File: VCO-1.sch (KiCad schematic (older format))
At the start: 72 parts

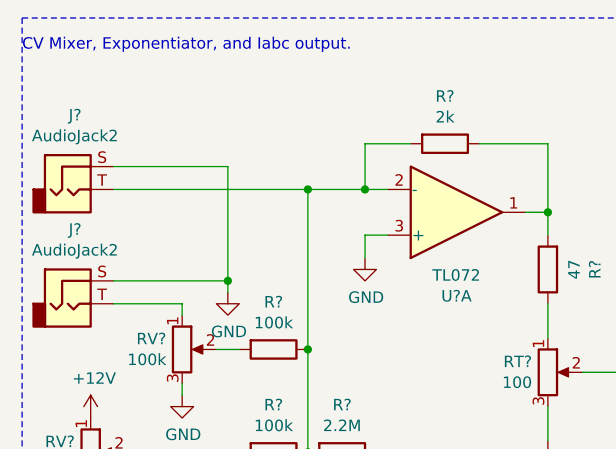
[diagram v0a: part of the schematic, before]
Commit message: Fixed missing input resistor for V/oct
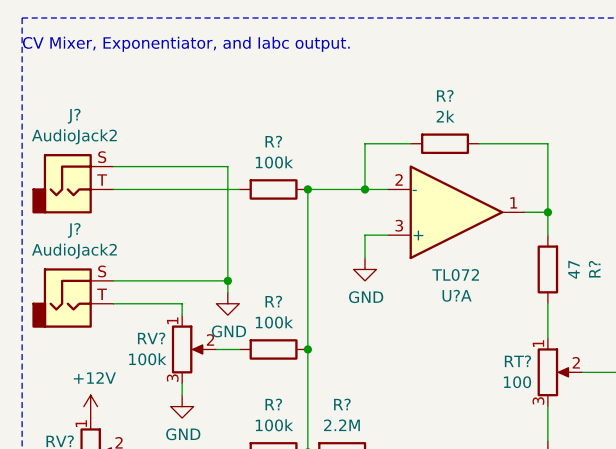
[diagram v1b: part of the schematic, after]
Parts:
- added R?: 100k, symbol Device:R
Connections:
- net at R?.1, R?.1, R?.1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: now also R?.1; no longer J?.T
- new net: J?.T, R?.2
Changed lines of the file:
@@
 	1    0    0    -1
 $EndComp
-Wire Wire Line
-	950  1550 1800 1550
 Connection ~ 1800 1550
 $Comp
@@
 Wire Wire Line
 	1450 1950 1450 2000
-Wire Wire Line
-	950  1450 1450 1450
-Wire Wire Line
-	1450 1450 1450 1950
-Connection ~ 1450 1950
 $Comp
 L power:GND #PWR?
@@
 Text Notes 10350 5450 0    50   ~ 0
 SAW OUT
+$Comp
+L Device:R R?
+U 1 1 604EF043
+P 1650 1550
+F 0 "R?" V 1443 1550 50  0000 C CNN
+F 1 "100k" V 1534 1550 50  0000 C CNN
+F 2 "" V 1580 1550 50  0001 C CNN
+F 3 "~" H 1650 1550 50  0001 C CNN
+	1    1650 1550
+	0    1    1    0
+$EndComp
+Wire Wire Line
+	950  1550 1500 1550
+Wire Wire Line
+	950  1450 1450 1450
+Wire Wire Line
+	1450 1450 1450 1950
+Connection ~ 1450 1950
 $EndSCHEMATC

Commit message: Board layed out
Silkscreen done, should be good for fab.
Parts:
- added J4: Conn_02x05_Odd_Even, Connector_PinHeader_2.54mm:PinHeader_2x05_P2.54mm_Vertical, symbol Connector_Generic:Conn_02x05_Odd_Even
- added R35: 2k +3500PPM, Resistor_THT:R_Axial_DIN0414_L11.9mm_D4.5mm_P15.24mm_Horizontal, symbol Device:R
- added unit 3 of U1
- added unit 2 of U2
- added unit 4 of U2
- added unit 5 of U2
- added unit 3 of U3
- added unit 3 of U4
- added unit 3 of U5
- C1: renamed from C?; footprint (none) -> Capacitor_THT:C_Rect_L10.3mm_W5.0mm_P7.50mm_MKS4
- C2, C3: renamed from C?; footprint (none) -> Capacitor_THT:C_Rect_L7.0mm_W4.5mm_P5.00mm
- C4: renamed from C?; footprint (none) -> Capacitor_THT:C_Rect_L4.0mm_W2.5mm_P2.50mm
- D1: renamed from D?; footprint (none) -> Diode_THT:D_T-1_P5.08mm_Horizontal
- D2, D3: renamed from D?; footprint (none) -> Diode_THT:D_DO-35_SOD27_P7.62mm_Horizontal
- J1, J2, J3, J5, J6, J7, J8: renamed from J?; footprint (none) -> Connector_Audio:Jack_3.5mm_QingPu_WQP-PJ398SM_Vertical_CircularHoles
- R1, R10, R11, R12, R13, R14, R15, R16, R17, R18, R19, R2, R20, R21, R22, R23, R24, R25, R26, R27, R28, R29, R3, R30, R31, R32, R33, R34, R4, R5, R6, R7, R8, R9: renamed from R?; footprint (none) -> Resistor_SMD:R_0805_2012Metric_Pad1.20x1.40mm_HandSolder
- RT1, RT2, RT3, RT4: renamed from RT?; footprint (none) -> Potentiometer_THT:Potentiometer_Bourns_3299W_Vertical
- RV1, RV2, RV3, RV4, RV5, RV6: renamed from RV?; footprint (none) -> Potentiometer_THT:Potentiometer_Alpha_RD901F-40-00D_Single_Vertical_CircularHoles
- U1, U3, U4, U5: renamed from U?; footprint (none) -> Package_SO:SOIC-8_3.9x4.9mm_P1.27mm
- U2: renamed from U?; value TL072 -> LM13700; footprint (none) -> Package_SO:SOIC-16_3.9x9.9mm_P1.27mm
- gave numbers to parts that had none: 4
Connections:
- net +12V: now also J4.1 (Pin_1), J4.2 (Pin_2), U1.8 (V+), U2.11 (V+), U3.8 (V+), U4.8 (V+), U5.8 (V+)
- net -12V: now also J4.10 (Pin_10), J4.9 (Pin_9), U1.4 (V-), U2.6 (V-), U3.4 (V-), U4.4 (V-), U5.4 (V-)
- net GND: now also J4.3 (Pin_3), J4.4 (Pin_4), J4.5 (Pin_5), J4.6 (Pin_6), J4.7 (Pin_7), J4.8 (Pin_8)
- net at R10.2, R8.1, U1.1: now also R35.1
- net at R3.1, R4.1, R5.1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: now also R35.2
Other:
- note added: "Alternative Tempco"
